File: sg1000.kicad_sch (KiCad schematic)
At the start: 77 parts, among them CN1 Conn_01x07_Female, J1 USB-B1HSB6, J2 RCJ-014, J3 RCJ-013, Q1 2n4401, Q1c1 2n3906, SW1 Pause Key, SW2 Power Toggle, SW3 Reset Key, U1 SG-1000-Cart, U100 74HCT574, U101 74HCT574, U102 74HCT574, U103 AS6C62256-DIP, U11 AS6C62256-DIP, U12 TMS9918A, U13 74LS139, U16 74LS32, U17 74LS14, U18 74LS257, U2 SG-1000-Expansion, U21 74LS257, U3 SN76489AN, U4 74LS32, U5 27C256, U6 74LS573, U7 74LS00, U9 Z80CPU, U99 74HCT04, X2 10.73863MHz

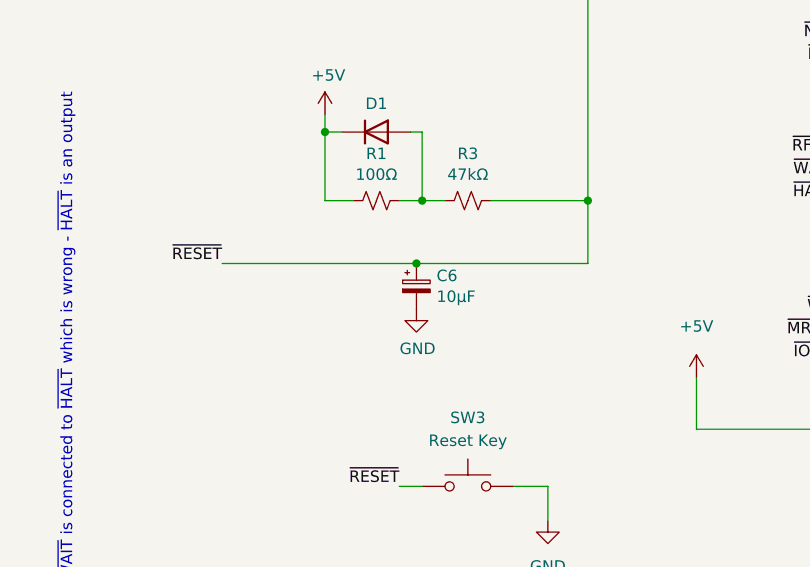
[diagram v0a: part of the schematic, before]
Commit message: Fix reset capacitor error
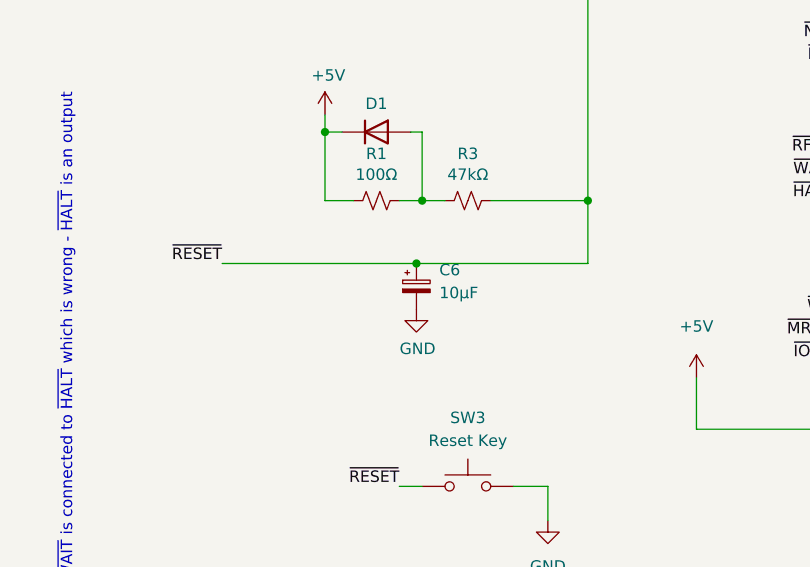
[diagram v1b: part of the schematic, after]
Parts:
- removed C6: 10µF, Capacitor_SMD:C_0805_2012Metric_Pad1.15x1.40mm_HandSolder, symbol Device:CP_Small
- added C6: 10µF, Capacitor_SMD:C_0805_2012Metric_Pad1.18x1.45mm_HandSolder, symbol Device:C_Polarized_Small
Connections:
- net GND: now also C6.2
- net ~{RESET}: now also C6.1
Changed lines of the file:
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@@
   (junction (at 157.48 557.53) (diameter 0) (color 0 0 0 0)
   )
+  (junction (at 247.65 83.82) (diameter 0) (color 0 0 0 0)
+  )
   (junction (at 453.39 58.42) (diameter 0) (color 0 0 0 0)
   )
@@
   (junction (at 177.165 165.735) (diameter 0) (color 0 0 0 0)
   )
-  (junction (at 247.65 83.82) (diameter 0) (color 0 0 0 0)
-  )
   (junction (at 248.285 76.835) (diameter 0) (color 0 0 0 0)
   )
@@
     (stroke (width 0) (type default) (color 0 0 0 0))
   )
+  (wire (pts (xy 247.65 83.82) (xy 266.7 83.82))
+    (stroke (width 0) (type default) (color 0 0 0 0))
+  )
   (wire (pts (xy 142.24 134.62) (xy 144.145 134.62))
     (stroke (width 0) (type default) (color 0 0 0 0))
@@
     (stroke (width 0) (type default) (color 0 0 0 0))
   )
-  (wire (pts (xy 266.7 83.82) (xy 247.65 83.82))
+  (wire (pts (xy 226.06 83.82) (xy 247.65 83.82))
     (stroke (width 0) (type default) (color 0 0 0 0))
   )
@@
     (stroke (width 0) (type default) (color 0 0 0 0))
   )
-  (wire (pts (xy 247.65 83.82) (xy 226.06 83.82))
-    (stroke (width 0) (type default) (color 0 0 0 0))
-  )
   (wire (pts (xy 144.145 83.82) (xy 142.875 83.82))
     (stroke (width 0) (type default) (color 0 0 0 0))
@@
     (pin "9")
   )
-  (symbol (lib_id "Device:CP_Small") (at 247.65 86.36 0) (unit 1)
-    (in_bom yes) (on_board yes)
-    (property "Reference" "C6" (id 0) (at 249.8852 85.1916 0)
-      (effects (font (size 1.27 1.27)) (justify left))
-    )
-    (property "Value" "10µF" (id 1) (at 249.8852 87.503 0)
-      (effects (font (size 1.27 1.27)) (justify left))
-    )
-    (property "Footprint" "Capacitor_SMD:C_0805_2012Metric_Pad1.15x1.40mm_HandSolder" (id 2) (at 247.65 86.36 0)
-      (effects (font (size 1.27 1.27)) hide)
-    )
-    (property "Datasheet" "~" (id 3) (at 247.65 86.36 0)
-      (effects (font (size 1.27 1.27)) hide)
-    )
-    (property "DigiKey" "1276-1298-1-ND" (id 4) (at 247.65 86.36 0)
-      (effects (font (size 1.27 1.27)) hide)
-    )
-    (pin "1")
-    (pin "2")
-  )
   (symbol (lib_id "power:GND") (at 247.65 88.9 0) (unit 1)
     (in_bom yes) (on_board yes)
@@
     (pin "9")
   )
+  (symbol (lib_id "Device:C_Polarized_Small") (at 247.65 86.36 0) (unit 1)
+    (in_bom yes) (on_board yes) (fields_autoplaced)
+    (property "Reference" "C6" (id 0) (at 250.19 84.5438 0)
+      (effects (font (size 1.27 1.27)) (justify left))
+    )
+    (property "Value" "10µF" (id 1) (at 250.19 87.0838 0)
+      (effects (font (size 1.27 1.27)) (justify left))
+    )
+    (property "Footprint" "Capacitor_SMD:C_0805_2012Metric_Pad1.18x1.45mm_HandSolder" (id 2) (at 247.65 86.36 0)
+      (effects (font (size 1.27 1.27)) hide)
+    )
+    (property "Datasheet" "~" (id 3) (at 247.65 86.36 0)
+      (effects (font (size 1.27 1.27)) hide)
+    )
+    (property "DigiKey" "1276-1298-1-ND" (id 4) (at 247.65 86.36 0)
+      (effects (font (size 1.27 1.27)) hide)
+    )
+    (pin "1")
+    (pin "2")
+  )
   (symbol (lib_id "power:GND") (at 270.51 180.34 0) (unit 1)
     (in_bom yes) (on_board yes) (fields_autoplaced)
@@
       (reference "C5") (unit 1) (value "220µF") (footprint "Capacitor_THT:CP_Radial_D6.3mm_P2.50mm")
     )
-    (path "/00000000-0000-0000-0000-0000621901d0"
-      (reference "C6") (unit 1) (value "10µF") (footprint "Capacitor_SMD:C_0805_2012Metric_Pad1.15x1.40mm_HandSolder")
+    (path "/cc87bb44-1522-4b98-b338-e8583fd0b43e"
+      (reference "C6") (unit 1) (value "10µF") (footprint "Capacitor_SMD:C_0805_2012Metric_Pad1.18x1.45mm_HandSolder")
     )
     (path "/00000000-0000-0000-0000-0000622404de"

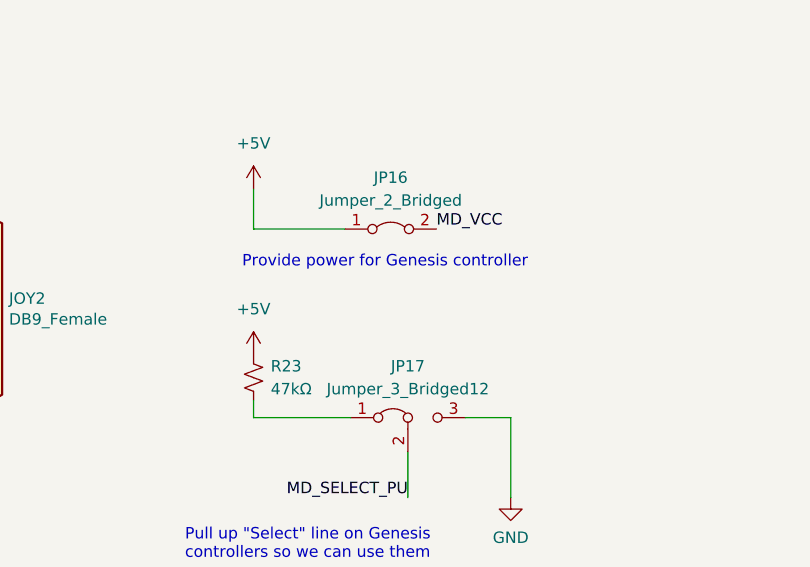
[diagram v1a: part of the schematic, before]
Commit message: Fix missing DigiKey part numbers for BOM
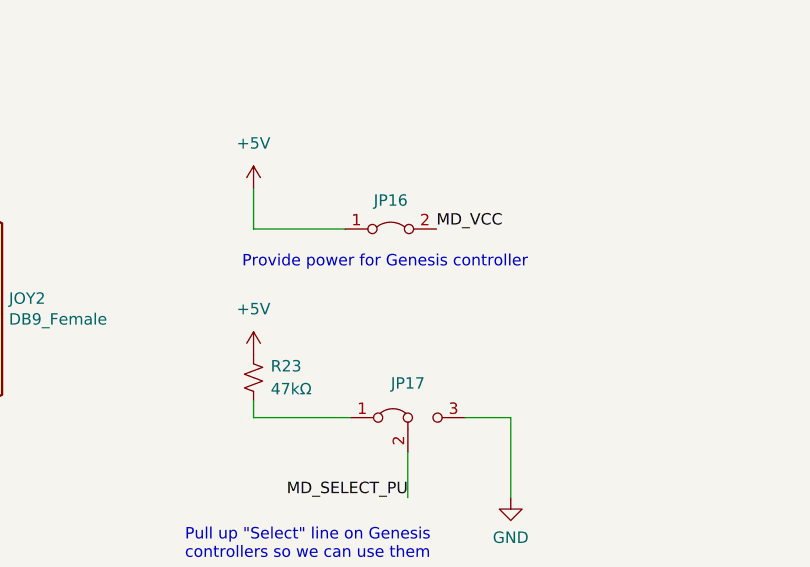
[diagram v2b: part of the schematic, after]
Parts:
- CN1, JP1, JP16, JP17, JP2, TP1, TP2, TP3, U2: now left out of the parts list
- R19, R20, R23: DigiKey (none) -> RMCF0805JT47K0CT-ND
- U17: footprint (none) -> Package_DIP:DIP-14_W7.62mm_Socket_LongPads
- U17: DigiKey (none) -> 296-1643-5-ND
- U6: DigiKey (none) -> DM74LS573N-ND
- U7: footprint Package_DIP:DIP-14_W7.62mm_Socket_LongPads -> (none)
- U7: DigiKey (none) -> 296-1626-ND
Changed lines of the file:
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@@
   )
   (symbol (lib_id "Connector:Conn_01x07_Female") (at 133.985 466.09 0) (unit 1)
-    (in_bom yes) (on_board yes)
+    (in_bom no) (on_board yes)
     (property "Reference" "CN1" (id 0) (at 134.6962 465.4296 0)
       (effects (font (size 1.27 1.27)) (justify left))
@@
     )
     (property "Datasheet" "74xx/74hc573.pdf" (id 3) (at 83.185 762.635 0)
+      (effects (font (size 1.27 1.27)) hide)
+    )
+    (property "DigiKey" "DM74LS573N-ND" (id 4) (at 83.185 762.635 0)
       (effects (font (size 1.27 1.27)) hide)
     )
@@
       (effects (font (size 1.27 1.27)) hide)
     )
+    (property "DigiKey" "RMCF0805JT47K0CT-ND" (id 4) (at 155.575 391.795 0)
+      (effects (font (size 1.27 1.27)) hide)
+    )
     (pin "1")
     (pin "2")
@@
   )
   (symbol (lib_id "Jumper:Jumper_3_Bridged12") (at 172.72 396.24 0) (unit 1)
-    (in_bom yes) (on_board yes) (fields_autoplaced)
-    (property "Reference" "JP17" (id 0) (at 172.72 390.525 0))
-    (property "Value" "Jumper_3_Bridged12" (id 1) (at 172.72 393.065 0))
+    (in_bom no) (on_board yes) (fields_autoplaced)
+    (property "Reference" "JP17" (id 0) (at 172.72 392.43 0))
+    (property "Value" "Jumper_3_Bridged12" (id 1) (at 172.72 393.065 0)
+      (effects (font (size 1.27 1.27)) hide)
+    )
     (property "Footprint" "Jumper:SolderJumper-3_P1.3mm_Bridged2Bar12_Pad1.0x1.5mm_NumberLabels" (id 2) (at 172.72 396.24 0)
       (effects (font (size 1.27 1.27)) hide)
@@
     (property "Reference" "U17" (id 0) (at 259.715 132.08 0))
     (property "Value" "74LS14" (id 1) (at 259.715 134.62 0))
-    (property "Footprint" "" (id 2) (at 259.715 141.605 0)
+    (property "Footprint" "Package_DIP:DIP-14_W7.62mm_Socket_LongPads" (id 2) (at 259.715 141.605 0)
       (effects (font (size 1.27 1.27)) hide)
     )
@@
       (effects (font (size 1.27 1.27)) hide)
     )
+    (property "DigiKey" "296-1643-5-ND" (id 4) (at 106.045 198.755 0)
+      (effects (font (size 1.27 1.27)) hide)
+    )
     (pin "14")
     (pin "7")
@@
   )
   (symbol (lib_id "Jumper:Jumper_2_Bridged") (at 170.815 375.285 0) (unit 1)
-    (in_bom yes) (on_board yes) (fields_autoplaced)
-    (property "Reference" "JP16" (id 0) (at 170.815 369.57 0))
-    (property "Value" "Jumper_2_Bridged" (id 1) (at 170.815 372.11 0))
+    (in_bom no) (on_board yes) (fields_autoplaced)
+    (property "Reference" "JP16" (id 0) (at 170.815 372.11 0))
+    (property "Value" "Jumper_2_Bridged" (id 1) (at 170.815 372.11 0)
+      (effects (font (size 1.27 1.27)) hide)
+    )
     (property "Footprint" "Jumper:SolderJumper-2_P1.3mm_Bridged_Pad1.0x1.5mm" (id 2) (at 170.815 375.285 0)
       (effects (font (size 1.27 1.27)) hide)
@@
     (property "Reference" "U17" (id 0) (at 294.005 142.24 0))
     (property "Value" "74LS14" (id 1) (at 294.005 144.78 0))
-    (property "Footprint" "" (id 2) (at 294.005 151.13 0)
+    (property "Footprint" "Package_DIP:DIP-14_W7.62mm_Socket_LongPads" (id 2) (at 294.005 151.13 0)
       (effects (font (size 1.27 1.27)) hide)
     )
@@
     (property "Reference" "U7" (id 0) (at 173.99 751.84 0))
     (property "Value" "74LS00" (id 1) (at 173.99 754.38 0))
-    (property "Footprint" "Package_DIP:DIP-14_W7.62mm_Socket_LongPads" (id 2) (at 173.99 761.365 0)
+    (property "Footprint" "" (id 2) (at 173.99 761.365 0)
       (effects (font (size 1.27 1.27)) hide)
     )
@@
     (property "Reference" "U7" (id 0) (at 193.04 744.22 0))
     (property "Value" "74LS00" (id 1) (at 193.04 746.76 0))
-    (property "Footprint" "Package_DIP:DIP-14_W7.62mm_Socket_LongPads" (id 2) (at 193.04 753.11 0)
+    (property "Footprint" "" (id 2) (at 193.04 753.11 0)
       (effects (font (size 1.27 1.27)) hide)
     )
@@
     (property "Reference" "U17" (id 0) (at 242.57 127 0))
     (property "Value" "74LS14" (id 1) (at 242.57 129.54 0))
-    (property "Footprint" "" (id 2) (at 242.57 135.89 0)
+    (property "Footprint" "Package_DIP:DIP-14_W7.62mm_Socket_LongPads" (id 2) (at 242.57 135.89 0)
       (effects (font (size 1.27 1.27)) hide)
     )
@@
       (effects (font (size 1.27 1.27)) (justify left))
     )
-    (property "Footprint" "Package_DIP:DIP-14_W7.62mm_Socket_LongPads" (id 2) (at 151.765 798.195 0)
+    (property "Footprint" "" (id 2) (at 151.765 798.195 0)
       (effects (font (size 1.27 1.27)) hide)
     )
@@
   )
   (symbol (lib_id "Connector:TestPoint") (at 458.47 67.31 180) (unit 1)
-    (in_bom yes) (on_board yes)
+    (in_bom no) (on_board yes)
     (property "Reference" "TP3" (id 0) (at 461.01 69.3419 0)
       (effects (font (size 1.27 1.27)) (justify right))
@@
   )
   (symbol (lib_id "Jumper:Jumper_2_Bridged") (at 27.305 695.96 0) (unit 1)
-    (in_bom yes) (on_board yes) (fields_autoplaced)
+    (in_bom no) (on_board yes) (fields_autoplaced)
     (property "Reference" "JP1" (id 0) (at 27.305 692.15 0))
     (property "Value" "Jumper_2_Bridged" (id 1) (at 27.305 692.15 0)
@@
   )
   (symbol (lib_id "LeadedSolder:SG-1000-Expansion") (at 160.02 535.94 0) (unit 1)
-    (in_bom yes) (on_board yes) (fields_autoplaced)
+    (in_bom no) (on_board yes) (fields_autoplaced)
     (property "Reference" "U2" (id 0) (at 160.7694 514.35 0)
       (effects (font (size 1.27 1.27)) (justify left))
@@
     (property "Reference" "U17" (id 0) (at 274.955 137.16 0))
     (property "Value" "74LS14" (id 1) (at 274.955 139.7 0))
-    (property "Footprint" "" (id 2) (at 274.955 146.685 0)
+    (property "Footprint" "Package_DIP:DIP-14_W7.62mm_Socket_LongPads" (id 2) (at 274.955 146.685 0)
       (effects (font (size 1.27 1.27)) hide)
     )
@@
     )
     (property "Datasheet" "~" (id 3) (at 106.68 769.62 0)
+      (effects (font (size 1.27 1.27)) hide)
+    )
+    (property "DigiKey" "RMCF0805JT47K0CT-ND" (id 4) (at 106.68 769.62 0)
       (effects (font (size 1.27 1.27)) hide)
     )
@@
       (effects (font (size 1.27 1.27)) hide)
     )
+    (property "DigiKey" "296-1626-ND" (id 4) (at 41.91 800.1 0)
+      (effects (font (size 1.27 1.27)) hide)
+    )
     (pin "1")
     (pin "2")
@@
       (effects (font (size 1.27 1.27)) hide)
     )
+    (property "DigiKey" "RMCF0805JT47K0CT-ND" (id 4) (at 102.87 760.095 0)
+      (effects (font (size 1.27 1.27)) hide)
+    )
     (pin "1")
     (pin "2")
   )
   (symbol (lib_id "Jumper:Jumper_2_Bridged") (at 27.305 707.39 0) (unit 1)
-    (in_bom yes) (on_board yes) (fields_autoplaced)
+    (in_bom no) (on_board yes) (fields_autoplaced)
     (property "Reference" "JP2" (id 0) (at 27.305 703.58 0))
     (property "Value" "Jumper_2_Bridged" (id 1) (at 27.305 703.58 0)
@@
   )
   (symbol (lib_id "Connector:TestPoint") (at 219.71 170.815 180) (unit 1)
-    (in_bom yes) (on_board yes) (fields_autoplaced)
+    (in_bom no) (on_board yes) (fields_autoplaced)
     (property "Reference" "TP1" (id 0) (at 222.25 172.8469 0)
       (effects (font (size 1.27 1.27)) (justify right))
@@
   )
   (symbol (lib_id "Connector:TestPoint") (at 434.34 67.31 180) (unit 1)
-    (in_bom yes) (on_board yes) (fields_autoplaced)
+    (in_bom no) (on_board yes) (fields_autoplaced)
     (property "Reference" "TP2" (id 0) (at 436.88 69.3419 0)
       (effects (font (size 1.27 1.27)) (justify right))
@@
     )
     (path "/920d71ed-1df7-4d0c-878d-ae98833f7fee"
-      (reference "U7") (unit 3) (value "74LS00") (footprint "Package_DIP:DIP-14_W7.62mm_Socket_LongPads")
+      (reference "U7") (unit 3) (value "74LS00") (footprint "")
     )
     (path "/96d1c762-0e9d-48c6-b857-612967edf253"
-      (reference "U7") (unit 4) (value "74LS00") (footprint "Package_DIP:DIP-14_W7.62mm_Socket_LongPads")
+      (reference "U7") (unit 4) (value "74LS00") (footprint "")
     )
     (path "/b886cb70-9abb-45ad-b882-d3561e7e2e9a"
-      (reference "U7") (unit 5) (value "74LS00") (footprint "Package_DIP:DIP-14_W7.62mm_Socket_LongPads")
+      (reference "U7") (unit 5) (value "74LS00") (footprint "")
     )
     (path "/9d8044f5-5b3d-4e3d-a53b-6503181a2d2c"
@@
     )
     (path "/9890ab0d-60be-401f-9610-601b07554a6a"
-      (reference "U17") (unit 3) (value "74LS14") (footprint "")
+      (reference "U17") (unit 3) (value "74LS14") (footprint "Package_DIP:DIP-14_W7.62mm_Socket_LongPads")
     )
     (path "/6402a45e-5c18-4acb-95d5-4d4add53b62f"
-      (reference "U17") (unit 4) (value "74LS14") (footprint "")
+      (reference "U17") (unit 4) (value "74LS14") (footprint "Package_DIP:DIP-14_W7.62mm_Socket_LongPads")
     )
     (path "/cabad2b3-d478-4de3-8c0a-6aca87ea2c66"
-      (reference "U17") (unit 5) (value "74LS14") (footprint "")
+      (reference "U17") (unit 5) (value "74LS14") (footprint "Package_DIP:DIP-14_W7.62mm_Socket_LongPads")
     )
     (path "/8e7b1928-223e-47d4-86c0-186f141f0453"
-      (reference "U17") (unit 6) (value "74LS14") (footprint "")
+      (reference "U17") (unit 6) (value "74LS14") (footprint "Package_DIP:DIP-14_W7.62mm_Socket_LongPads")
     )
     (path "/7694c0b2-929f-4a6b-9d1a-50ef57c75725"

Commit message: Boot ROM ZIF
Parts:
- U5: footprint Package_DIP:DIP-28_W15.24mm -> LeadedSolder:DIP-28_W15.24mm_ZIF_Pads
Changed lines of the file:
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@@
       (effects (font (size 1.27 1.27)) (justify left))
     )
-    (property "Footprint" "Package_DIP:DIP-28_W15.24mm" (id 2) (at 61.595 681.355 0)
+    (property "Footprint" "LeadedSolder:DIP-28_W15.24mm_ZIF_Pads" (id 2) (at 61.595 681.355 0)
       (effects (font (size 1.27 1.27)) hide)
     )
@@
     )
     (path "/ff991c36-e6d2-4301-a90b-2c025ba4a1f0"
-      (reference "U5") (unit 1) (value "27C256") (footprint "Package_DIP:DIP-28_W15.24mm")
+      (reference "U5") (unit 1) (value "27C256") (footprint "LeadedSolder:DIP-28_W15.24mm_ZIF_Pads")
     )
     (path "/02bf6642-3f14-4e79-aba5-8a32820b8438"

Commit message: Force footprint on U7
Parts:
- U7: footprint (none) -> Package_DIP:DIP-14_W7.62mm_Socket_LongPads
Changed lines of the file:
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@@
     (property "Reference" "U7" (id 0) (at 173.99 751.84 0))
     (property "Value" "74LS00" (id 1) (at 173.99 754.38 0))
-    (property "Footprint" "" (id 2) (at 173.99 761.365 0)
+    (property "Footprint" "Package_DIP:DIP-14_W7.62mm_Socket_LongPads" (id 2) (at 173.99 761.365 0)
       (effects (font (size 1.27 1.27)) hide)
     )
@@
     (property "Reference" "U7" (id 0) (at 193.04 744.22 0))
     (property "Value" "74LS00" (id 1) (at 193.04 746.76 0))
-    (property "Footprint" "" (id 2) (at 193.04 753.11 0)
+    (property "Footprint" "Package_DIP:DIP-14_W7.62mm_Socket_LongPads" (id 2) (at 193.04 753.11 0)
       (effects (font (size 1.27 1.27)) hide)
     )
@@
       (effects (font (size 1.27 1.27)) (justify left))
     )
-    (property "Footprint" "" (id 2) (at 151.765 798.195 0)
+    (property "Footprint" "Package_DIP:DIP-14_W7.62mm_Socket_LongPads" (id 2) (at 151.765 798.195 0)
       (effects (font (size 1.27 1.27)) hide)
     )
@@
     (property "Reference" "U7" (id 0) (at 41.91 791.21 0))
     (property "Value" "74LS00" (id 1) (at 41.91 793.75 0))
-    (property "Footprint" "" (id 2) (at 41.91 800.1 0)
+    (property "Footprint" "Package_DIP:DIP-14_W7.62mm_Socket_LongPads" (id 2) (at 41.91 800.1 0)
       (effects (font (size 1.27 1.27)) hide)
     )
@@
     )
     (path "/edfd2681-1660-471b-a1d2-c3d43b997978"
-      (reference "U7") (unit 1) (value "74LS00") (footprint "")
+      (reference "U7") (unit 1) (value "74LS00") (footprint "Package_DIP:DIP-14_W7.62mm_Socket_LongPads")
     )
     (path "/920d71ed-1df7-4d0c-878d-ae98833f7fee"
-      (reference "U7") (unit 3) (value "74LS00") (footprint "")
+      (reference "U7") (unit 3) (value "74LS00") (footprint "Package_DIP:DIP-14_W7.62mm_Socket_LongPads")
     )
     (path "/96d1c762-0e9d-48c6-b857-612967edf253"
-      (reference "U7") (unit 4) (value "74LS00") (footprint "")
+      (reference "U7") (unit 4) (value "74LS00") (footprint "Package_DIP:DIP-14_W7.62mm_Socket_LongPads")
     )
     (path "/b886cb70-9abb-45ad-b882-d3561e7e2e9a"
-      (reference "U7") (unit 5) (value "74LS00") (footprint "")
+      (reference "U7") (unit 5) (value "74LS00") (footprint "Package_DIP:DIP-14_W7.62mm_Socket_LongPads")
     )
     (path "/9d8044f5-5b3d-4e3d-a53b-6503181a2d2c"

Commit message: Digi-Key part numbers for 10k, 100k that were missing them
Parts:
- R18, R21: DigiKey (none) -> RMCF0805JT10K0CT-ND
- R22: DigiKey (none) -> RMCF0805FT100KCT-ND
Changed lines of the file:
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@@
+      (effects (font (size 1.27 1.27)) hide)
+    )
+    (property "DigiKey" "RMCF0805JT10K0CT-ND" (id 4) (at 86.868 627.888 0)
       (effects (font (size 1.27 1.27)) hide)
     )
@@
     )
     (property "Datasheet" "~" (id 3) (at 170.18 165.735 0)
+      (effects (font (size 1.27 1.27)) hide)
+    )
+    (property "DigiKey" "RMCF0805FT100KCT-ND" (id 4) (at 170.18 165.735 0)
       (effects (font (size 1.27 1.27)) hide)
     )
@@
       (effects (font (size 1.27 1.27)) hide)
     )
+    (property "DigiKey" "RMCF0805JT10K0CT-ND" (id 4) (at 165.1 156.21 0)
+      (effects (font (size 1.27 1.27)) hide)
+    )
